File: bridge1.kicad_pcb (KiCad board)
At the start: 2 copper layers, 64 x 50 mm, 13 parts, among them J1 Conn_01x04, U1 pico

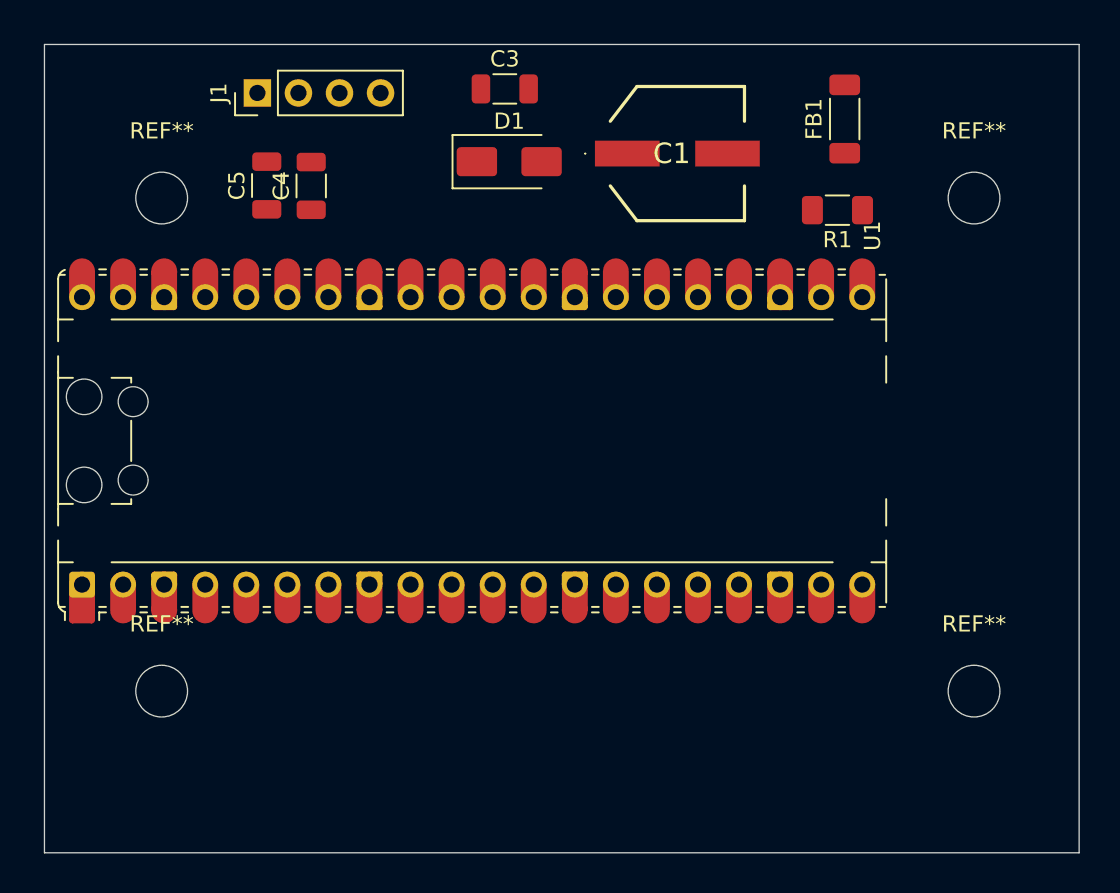
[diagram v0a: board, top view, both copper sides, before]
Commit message: Updated schematic and PCB files, have full layout now.
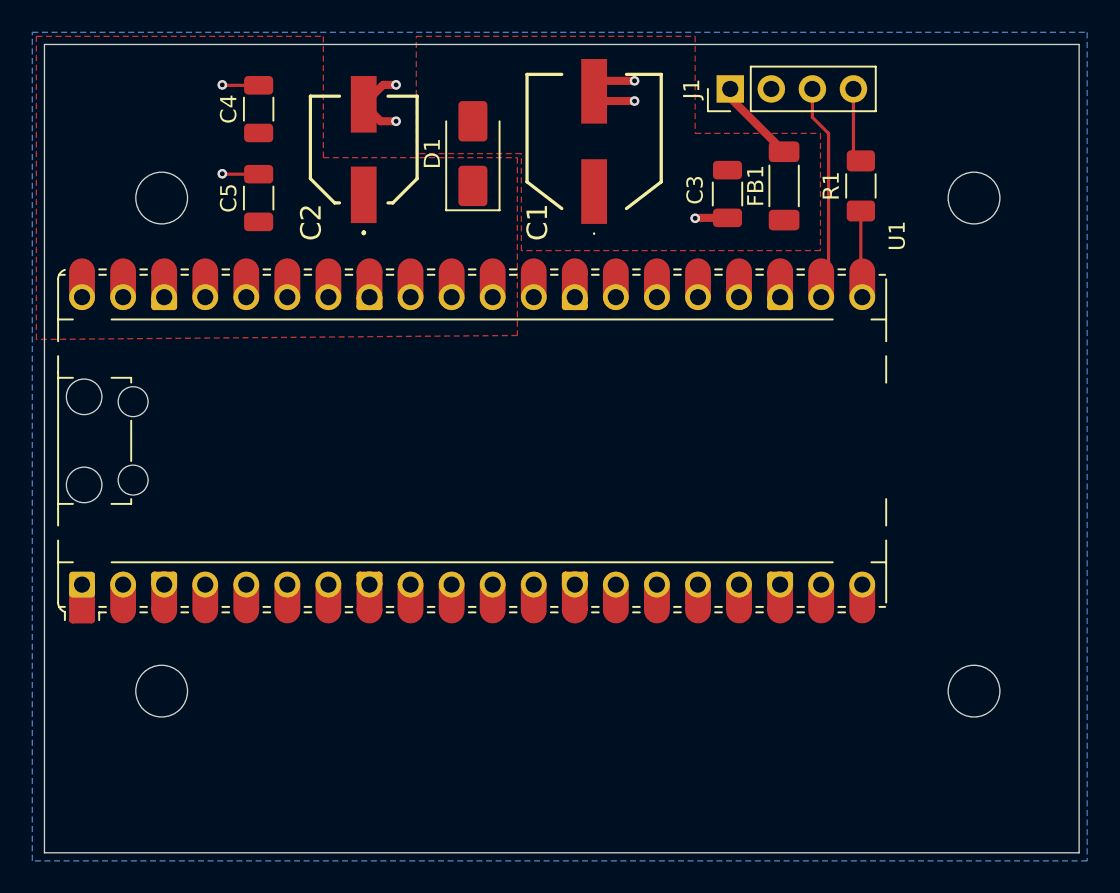
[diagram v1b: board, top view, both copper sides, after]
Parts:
- added C2: 100uF, Wayne:16SVF180M, F.Cu at (195.8, 52.2)
- moved J1 29.3 mm to (218.4, 48.5)
- moved C3 15.2 mm to (218.2, 55.0), turned to -90 degrees
- moved C4 5.76 mm to (189.2, 49.8)
- moved FB1 5.58 mm to (221.8, 54.5)
- moved C1 5.20 mm to (210.0, 51.8), turned to 90 degrees
- moved D1 2.30 mm to (202.5, 52.5), turned to 90 degrees
- moved R1 2.09 mm to (226.5, 54.5), turned to 90 degrees
- moved C5 0.92 mm to (189.2, 55.2)
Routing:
- net GND: track 0.00 -> 17.0 mm, vias 0 -> 7
- net /uart_rx: track 0.00 -> 12.7 mm
- net Net-(J1-Pin_1): track 0.00 -> 5.27 mm
- net /uart_tx: track 0.00 -> 4.64 mm
- net Net-(U1-GP16): track 0.00 -> 4.57 mm
- added copper zone on B.Cu, net GND
- added copper zone on F.Cu, net Net-(D1-A)
- added copper zone on F.Cu, net Net-(D1-K)
